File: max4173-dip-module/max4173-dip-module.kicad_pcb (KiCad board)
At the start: 2 copper layers, 7.6 x 10.2 mm, 5 parts, among them K1 CONN_3, K2 CONN_3, U1 MAX4173_SO8

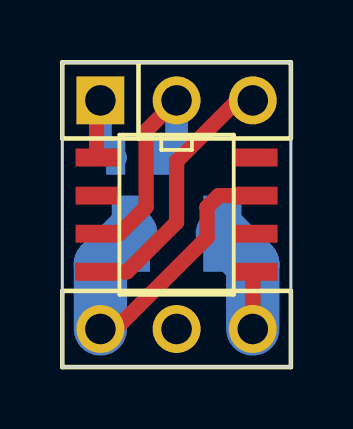
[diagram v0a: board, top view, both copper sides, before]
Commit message: fixed pin numbering error on MAX4173 board
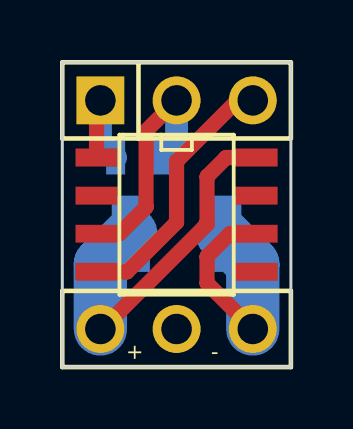
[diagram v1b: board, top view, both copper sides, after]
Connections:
- K2 pad 1: /RS+ -> /RS-
- K2 pad 3: /RS- -> /RS+
- R1 pad 1: /RS- -> /RS+
- R1 pad 2: /RS+ -> /RS-
- U1 pad 5: /RS+ -> (no net)
- U1 pad 6: (no net) -> /RS-
- U1 pad 7: /RS- -> (no net)
- U1 pad 8: (no net) -> /RS+
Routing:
- net /RS+: track 5.55 -> 12.1 mm
- net /RS-: track 11.2 -> 8.61 mm
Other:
- net class Default: trace_width 0.762 -> 0.508
- board text added: "+"
- board text added: "-"
- board text added: "v2"
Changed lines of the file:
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@@
     (area 140.639799 60.5028 148.920201 74.1172)
     (thickness 1.6)
-    (drawings 4)
-    (tracks 26)
+    (drawings 7)
+    (tracks 28)
     (zones 0)
     (modules 5)
@@
   (page A3)
   (layers
-    (15 F.Cu signal)
-    (0 B.Cu signal)
+    (15 F.Cu signal hide)
+    (0 B.Cu signal hide)
     (18 B.Paste user)
     (19 F.Paste user)
@@
   )
   (setup
-    (last_trace_width 0.762)
+    (last_trace_width 0.508)
     (trace_clearance 0.254)
     (zone_clearance 0.508)
@@
   (net_class Default "This is the default net class."
     (clearance 0.254)
-    (trace_width 0.762)
+    (trace_width 0.508)
     (via_dia 0.889)
     (via_drill 0.635)
@@
     (pad 1 thru_hole circle (at -2.54 0 180) (size 1.6002 1.6002) (drill 1.016)
       (layers *.Cu *.Mask F.SilkS)
+      (net 4 /RS-)
+    )
+    (pad 2 thru_hole circle (at 0 0 180) (size 1.6002 1.6002) (drill 1.016)
+      (layers *.Cu *.Mask F.SilkS)
+    )
+    (pad 3 thru_hole circle (at 2.54 0 180) (size 1.6002 1.6002) (drill 1.016)
+      (layers *.Cu *.Mask F.SilkS)
       (net 3 /RS+)
-    )
-    (pad 2 thru_hole circle (at 0 0 180) (size 1.6002 1.6002) (drill 1.016)
-      (layers *.Cu *.Mask F.SilkS)
-    )
-    (pad 3 thru_hole circle (at 2.54 0 180) (size 1.6002 1.6002) (drill 1.016)
-      (layers *.Cu *.Mask F.SilkS)
-      (net 4 /RS-)
     )
     (model pin_array/pins_array_3x1.wrl
@@
     (pad 8 smd rect (at -1.905 -2.667 270) (size 0.59944 1.39954)
       (layers F.Cu F.Paste F.Mask)
+      (net 3 /RS+)
     )
     (pad 1 smd rect (at -1.905 2.667 270) (size 0.59944 1.39954)
@@
     (pad 7 smd rect (at -0.635 -2.667 270) (size 0.59944 1.39954)
       (layers F.Cu F.Paste F.Mask)
+    )
+    (pad 6 smd rect (at 0.635 -2.667 270) (size 0.59944 1.39954)
+      (layers F.Cu F.Paste F.Mask)
       (net 4 /RS-)
     )
-    (pad 6 smd rect (at 0.635 -2.667 270) (size 0.59944 1.39954)
-      (layers F.Cu F.Paste F.Mask)
-    )
     (pad 5 smd rect (at 1.905 -2.667 270) (size 0.59944 1.39954)
       (layers F.Cu F.Paste F.Mask)
-      (net 3 /RS+)
     )
     (pad 2 smd rect (at -0.635 2.667 270) (size 0.59944 1.39954)
@@
     (pad 1 smd rect (at -1.524 0) (size 1.27 2.54)
       (layers B.Cu B.Paste B.Mask)
-      (net 4 /RS-)
+      (net 3 /RS+)
     )
     (pad 2 smd rect (at 1.524 0) (size 1.27 2.54)
       (layers B.Cu B.Paste B.Mask)
-      (net 3 /RS+)
+      (net 4 /RS-)
     )
     (model smd/chip_cms.wrl
@@
       (rotate (xyz 0 0 0))
     )
+  )
+  (gr_text - (at 146.05 71.882) (layer F.SilkS)
+    (effects (font (size 0.508 0.508) (thickness 0.127)))
+  )
+  (gr_text + (at 143.383 71.882) (layer F.SilkS)
+    (effects (font (size 0.508 0.508) (thickness 0.127)))
+  )
+  (gr_text v2 (at 147.828 69.088 90) (layer B.SilkS)
+    (effects (font (size 0.508 0.508) (thickness 0.127)) (justify mirror))
   )
   (gr_line (start 140.97 72.39) (end 140.97 62.23) (angle 90) (layer Edge.Cuts) (width 0.1))
@@
   (segment (start 144.78 67.564) (end 144.78 65.532) (width 0.508) (layer F.Cu) (net 2))
   (segment (start 143.129 69.215) (end 144.78 67.564) (width 0.508) (layer F.Cu) (net 2))
-  (segment (start 147.32 71.12) (end 147.32 68.961) (width 1.778) (layer B.Cu) (net 3))
-  (segment (start 147.32 68.961) (end 146.304 67.945) (width 1.778) (layer B.Cu) (net 3))
-  (segment (start 147.32 71.12) (end 147.32 69.342) (width 0.508) (layer F.Cu) (net 3))
-  (segment (start 147.32 69.342) (end 147.447 69.215) (width 0.508) (layer F.Cu) (net 3))
-  (segment (start 142.24 71.12) (end 142.24 68.961) (width 1.778) (layer B.Cu) (net 4))
-  (segment (start 142.24 68.961) (end 143.256 67.945) (width 1.778) (layer B.Cu) (net 4))
-  (segment (start 142.24 71.12) (end 142.748 71.12) (width 0.508) (layer F.Cu) (net 4))
-  (segment (start 146.177 66.675) (end 147.447 66.675) (width 0.508) (layer F.Cu) (net 4))
-  (segment (start 145.796 67.056) (end 146.177 66.675) (width 0.508) (layer F.Cu) (net 4))
-  (segment (start 145.796 68.072) (end 145.796 67.056) (width 0.508) (layer F.Cu) (net 4))
-  (segment (start 142.748 71.12) (end 145.796 68.072) (width 0.508) (layer F.Cu) (net 4))
+  (segment (start 142.24 71.12) (end 142.301634 71.12) (width 0.508) (layer F.Cu) (net 3) (status C00000))
+  (segment (start 146.431 65.405) (end 147.447 65.405) (width 0.508) (layer F.Cu) (net 3) (status 800000))
+  (segment (start 145.796 66.04) (end 146.431 65.405) (width 0.508) (layer F.Cu) (net 3))
+  (segment (start 145.796 67.625634) (end 145.796 66.04) (width 0.508) (layer F.Cu) (net 3))
+  (segment (start 142.301634 71.12) (end 145.796 67.625634) (width 0.508) (layer F.Cu) (net 3) (status 400000))
+  (segment (start 142.24 71.12) (end 142.24 68.961) (width 1.778) (layer B.Cu) (net 3))
+  (segment (start 142.24 68.961) (end 143.256 67.945) (width 1.778) (layer B.Cu) (net 3))
+  (segment (start 147.447 67.945) (end 146.554268 67.945) (width 0.508) (layer F.Cu) (net 4) (status 400000))
+  (segment (start 145.796 69.596) (end 147.32 71.12) (width 0.508) (layer F.Cu) (net 4) (status 800000))
+  (segment (start 145.796 68.703268) (end 145.796 69.596) (width 0.508) (layer F.Cu) (net 4))
+  (segment (start 146.554268 67.945) (end 145.796 68.703268) (width 0.508) (layer F.Cu) (net 4))
+  (segment (start 147.32 71.12) (end 147.32 68.961) (width 1.778) (layer B.Cu) (net 4))
+  (segment (start 147.32 68.961) (end 146.304 67.945) (width 1.778) (layer B.Cu) (net 4))
   (segment (start 142.24 63.5) (end 142.24 64.897) (width 0.762) (layer B.Cu) (net 5))
   (segment (start 142.24 64.897) (end 142.748 65.405) (width 0.762) (layer B.Cu) (net 5))
